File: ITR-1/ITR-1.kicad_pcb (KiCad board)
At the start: 2 copper layers, 30 x 45 mm, 45 parts, among them K1 Кнопка_KLS7-TS5401-1.35-250-T, X1 отверстие_под_пайку, X2 отверстие_под_пайку

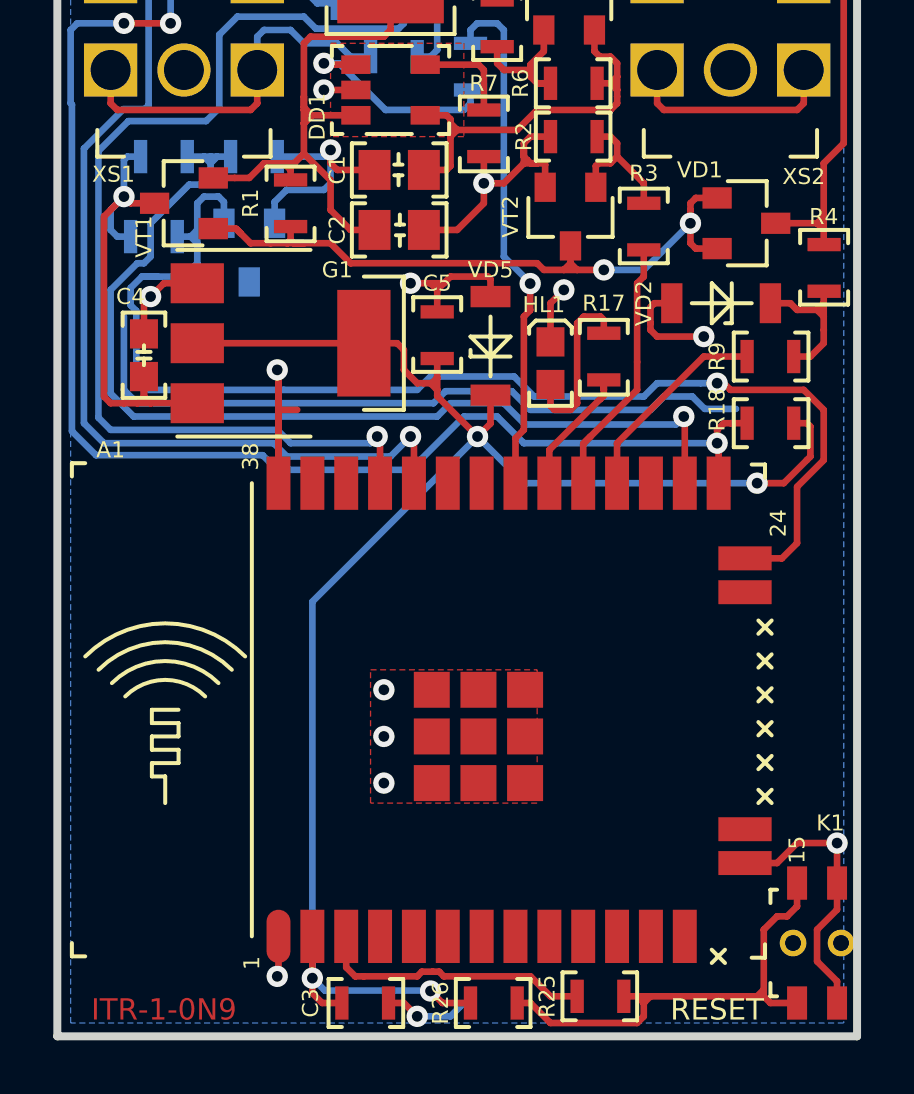
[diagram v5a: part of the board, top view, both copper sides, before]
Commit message: причесана трассировка +PDF +GBR
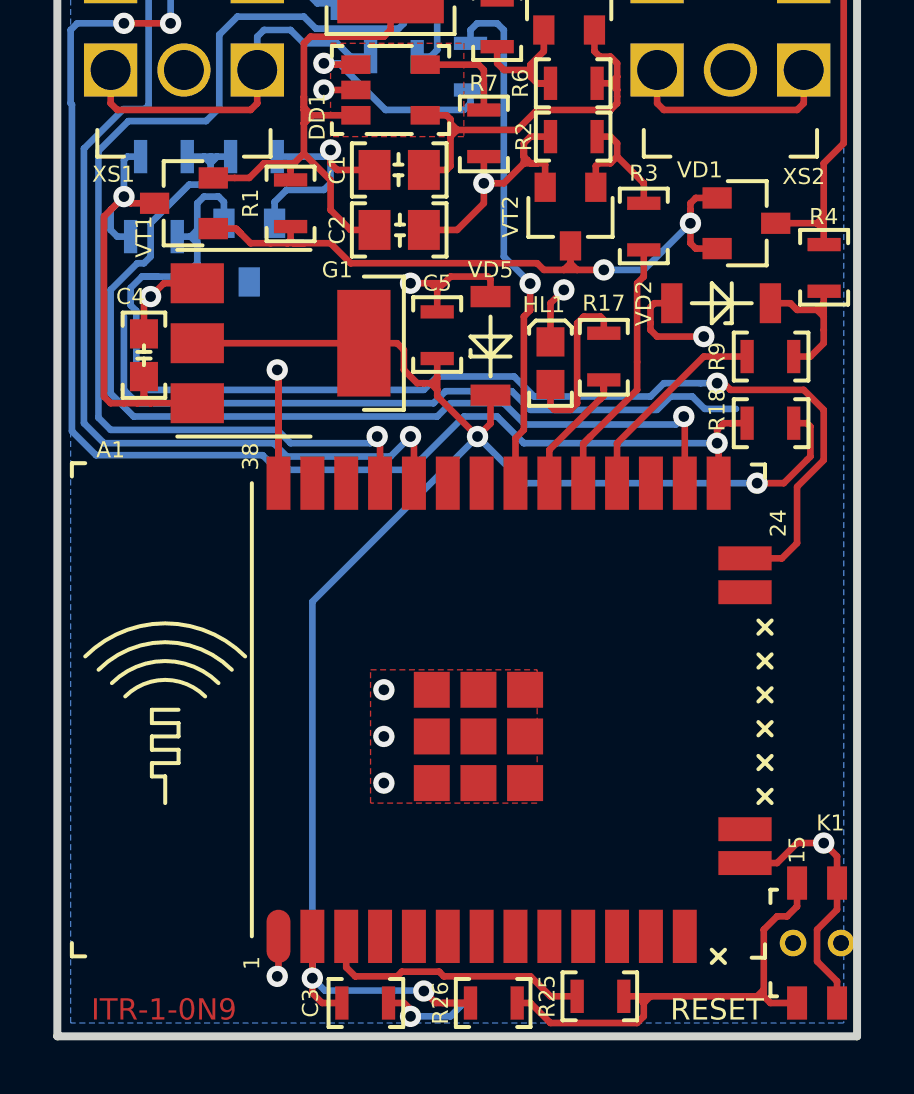
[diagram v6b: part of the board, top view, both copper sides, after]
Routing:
- net /3V3: track 64.0 -> 65.3 mm
- net /GND: track 101.4 -> 100.7 mm

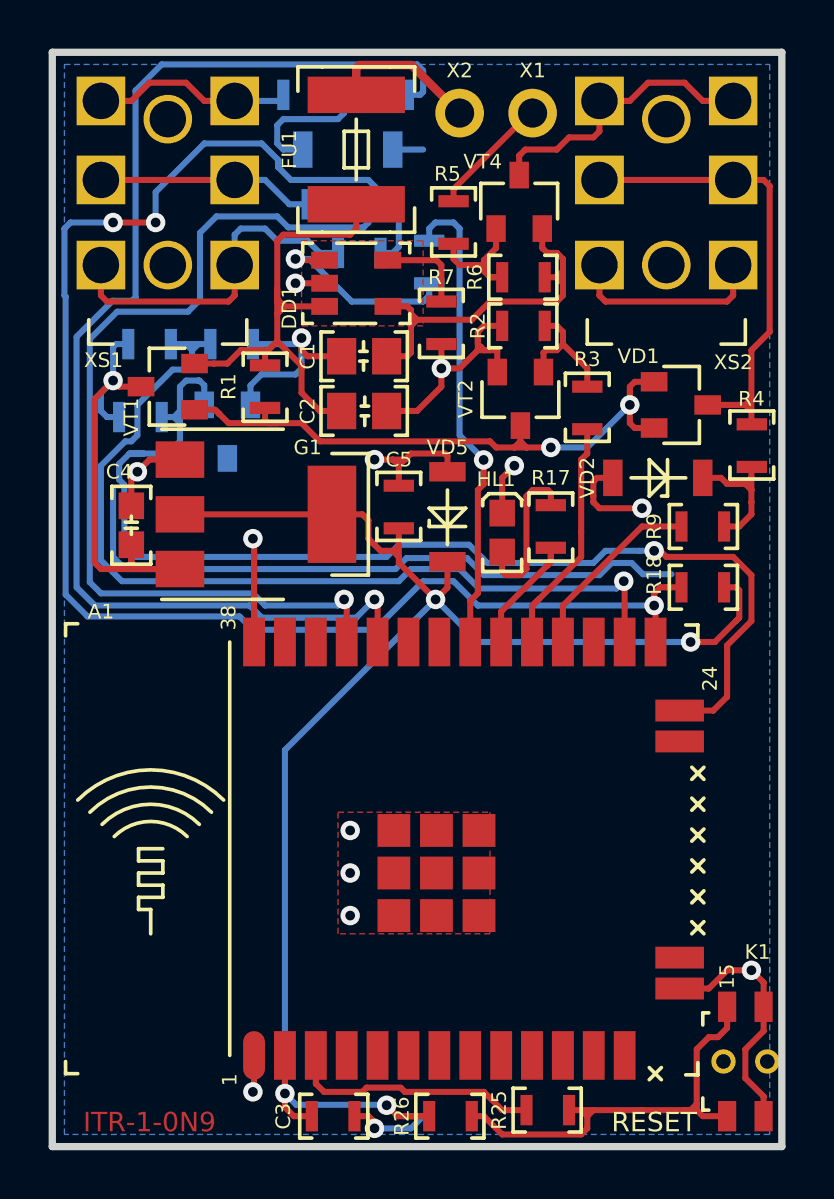
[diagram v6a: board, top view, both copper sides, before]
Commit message: добавлена кнопка воот, перенесен Ain, начато BT arduino
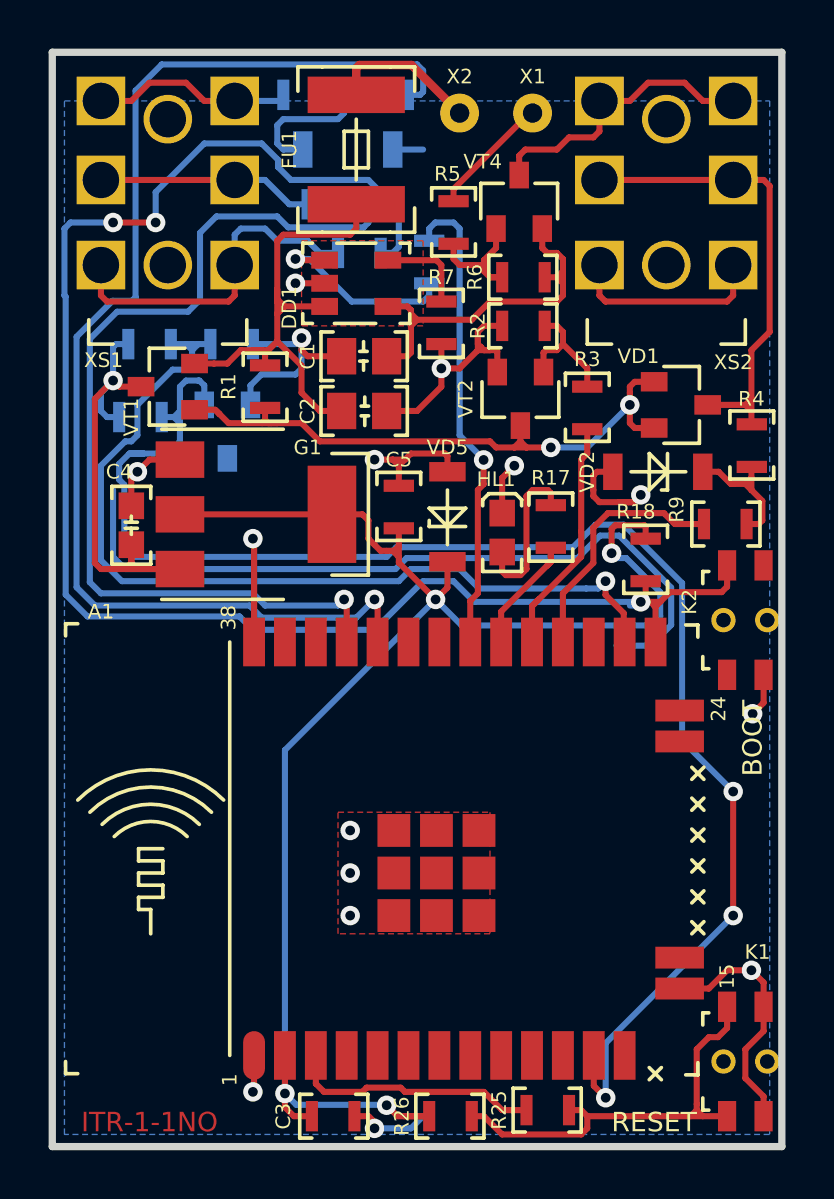
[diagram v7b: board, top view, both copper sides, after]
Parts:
- added K2: Кнопка_KLS7-TS5401-1.35-250-T, N_X:Кнопка_KLS7-TS5401, F.Cu at (129.2, 80.6)
- moved R18 2.61 mm to (124.4, 75.9), turned to 90 degrees
- moved R9 0.93 mm to (127.7, 74.4)
- moved VD2 0.25 mm to (123.0, 72.2)
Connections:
- A1 pad 12: (no net) -> /AN.2V5.REF
- A1 pad 24: /AN.2V5.REF -> (no net)
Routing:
- net /AN.2V5.REF: track 47.2 -> 63.3 mm, vias 1 -> 3
- net /GND: track 100.7 -> 107.9 mm, vias 14 -> 15
- net /BOOT: track 63.7 -> 67.7 mm
- net /BUTT.TURN: track 7.72 -> 10.2 mm
- net /3V3: track 65.3 -> 66.5 mm
- net Net-(K1-Pad1): track 18.6 -> 18.0 mm
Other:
- board text added: "ITR-1-1NO"
- board text removed: "ITR-1-0N9"

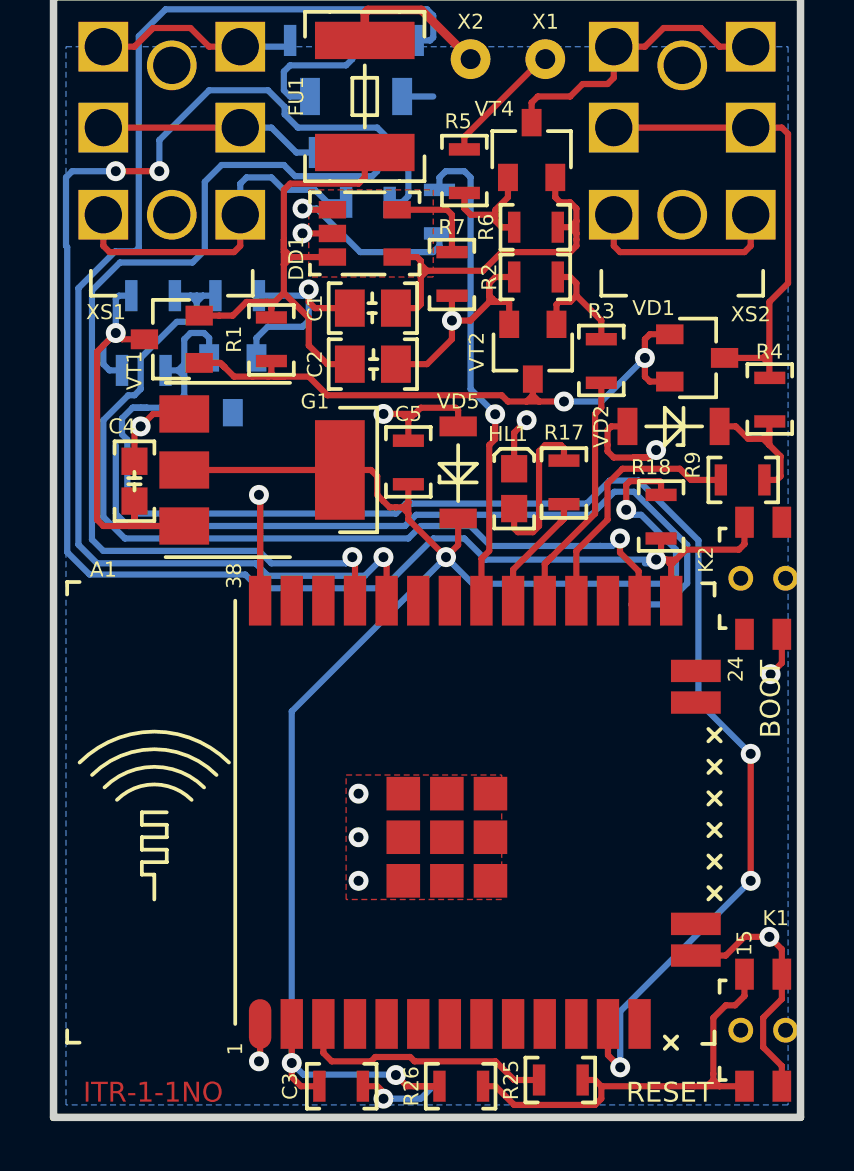
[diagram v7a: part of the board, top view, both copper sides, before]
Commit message: заменен LDO на самопальный, уменьшена заливки, убраны дорожки под PCB
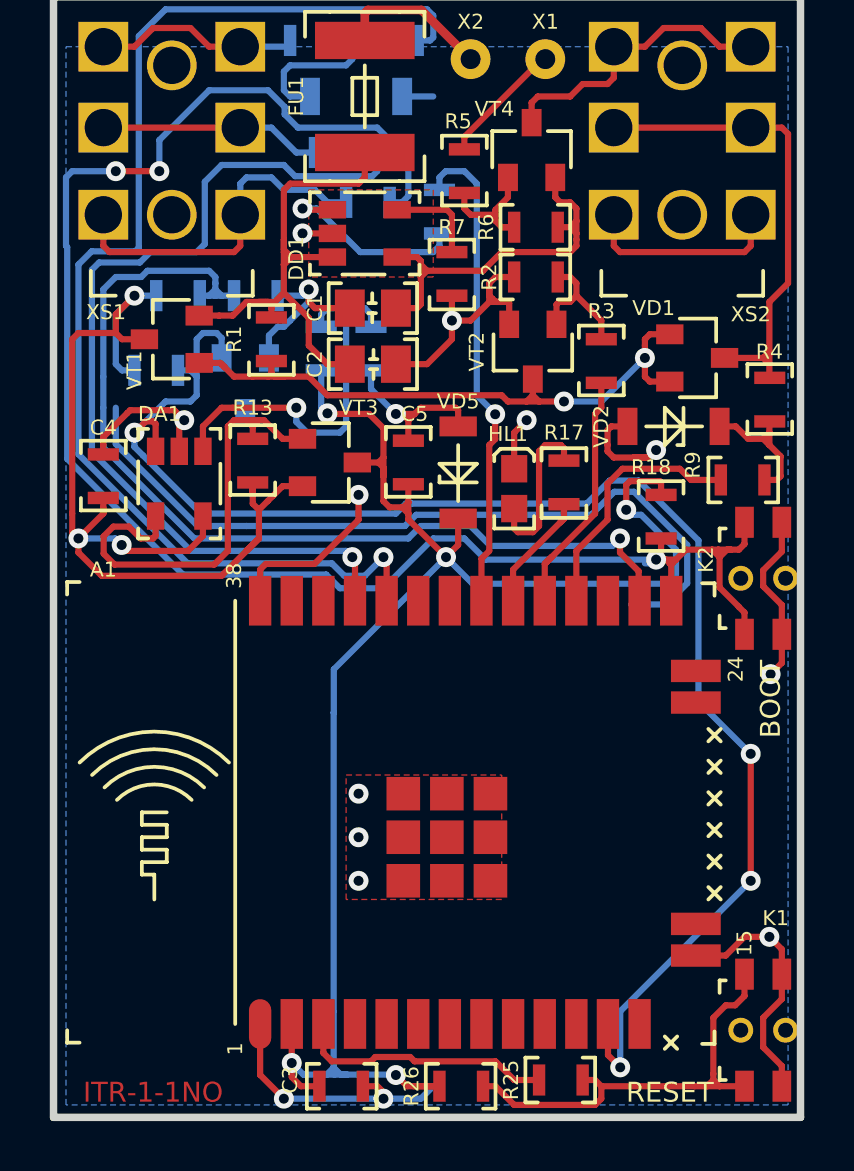
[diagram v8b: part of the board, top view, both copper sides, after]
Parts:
- removed G1: стабилизатор_нерегулируемый_LM1117S33-SOT223, N_VD_HL:Транзистор_NPN_SOT223
- added DA1: ОУ_LMV321ILT, N_G:SOT-23-5_pnp, F.Cu at (105.0, 74.5)
- added R13: Резистор_0,065Вт, N_RLC:Резистор_SMD_0603_0,065_Вт, F.Cu at (108.0, 73.6)
- added R14: Резистор_0,065Вт, N_RLC:Резистор_SMD_0603_0,065_Вт, B.Cu at (110.8, 69.1)
- added R15: Резистор_0,065Вт, N_RLC:Резистор_SMD_0603_0,065_Вт, B.Cu at (112.8, 69.1)
- added VT3: Транзистор_полевой_P-канал(IRLML2246TRPBF), N_VD_HL:Транзистор_IRLML6344TR_SOT-23, F.Cu at (111.1, 73.7)
- C4: footprint N_RLC:Конденсатор_SMD_IEC_0603 -> N_RLC:Конденсатор_SMD_0603_pnp
- moved C4 1.27 mm to (102.0, 74.2)
- moved R10 1.00 mm to (105.0, 67.0)
- moved R11 0.75 mm to (108.1, 67.0)
- moved G2 0.50 mm to (107.7, 70.6)
- moved R12 0.50 mm to (104.1, 70.0)
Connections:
- A1 pad 10: (no net) -> Net-(A1-Pad10)
- A1 pad 11: (no net) -> Net-(A1-Pad11)
- A1 pad 13: (no net) -> Net-(A1-Pad13)
- A1 pad 16: (no net) -> Net-(A1-Pad16)
- A1 pad 23: (no net) -> Net-(A1-Pad23)
- A1 pad 24: (no net) -> Net-(A1-Pad24)
- A1 pad 27: (no net) -> Net-(A1-Pad27)
- A1 pad 32: (no net) -> Net-(A1-Pad32)
- A1 pad 33: (no net) -> Net-(A1-Pad33)
- A1 pad 36: (no net) -> Net-(A1-Pad36)
- A1 pad 37: (no net) -> Net-(A1-Pad37)
- A1 pad 4: (no net) -> Net-(A1-Pad4)
- A1 pad 5: (no net) -> Net-(A1-Pad5)
- A1 pad 6: (no net) -> Net-(A1-Pad6)
- A1 pad 7: (no net) -> Net-(A1-Pad7)
- A1 pad 8: (no net) -> Net-(A1-Pad8)
- A1 pad 9: (no net) -> Net-(A1-Pad9)
- G2 pad 3: (no net) -> Net-(G2-Pad3)
- K2 pad 1: (no net) -> /BOOT
- K2 pad 3: (no net) -> /GND
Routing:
- net /BAT.LOAD: track 19.0 -> 41.6 mm, vias 1 -> 3
- net Net-(DA1-Pad4): track 0.00 -> 18.8 mm
- net Net-(DA1-Pad1): track 0.00 -> 16.8 mm, vias 0 -> 1
- net /GND: track 107.9 -> 119.9 mm
- net /BOOT: track 67.7 -> 70.3 mm
- net /UART.TX: track 39.5 -> 37.6 mm
- net /AN.BAT.MEASURE: track 37.9 -> 39.8 mm
- net /UART.RX: track 50.7 -> 49.1 mm
- net /3V3: track 66.5 -> 67.4 mm, vias 4 -> 5
- net /AN.2V5.REF: track 63.3 -> 62.8 mm, vias 3 -> 4
